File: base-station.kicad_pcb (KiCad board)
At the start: 2 copper layers, 85.7 x 87.2 mm, 53 parts, among them IC1 ATMEGA32-A, P1 HC-05, P2 NRF24L01+, P3 SERIAL, P4 LCD1, P5 LCD1, P6 POWER, Q1 BTEN, SW1 RESET, U1 LP5907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

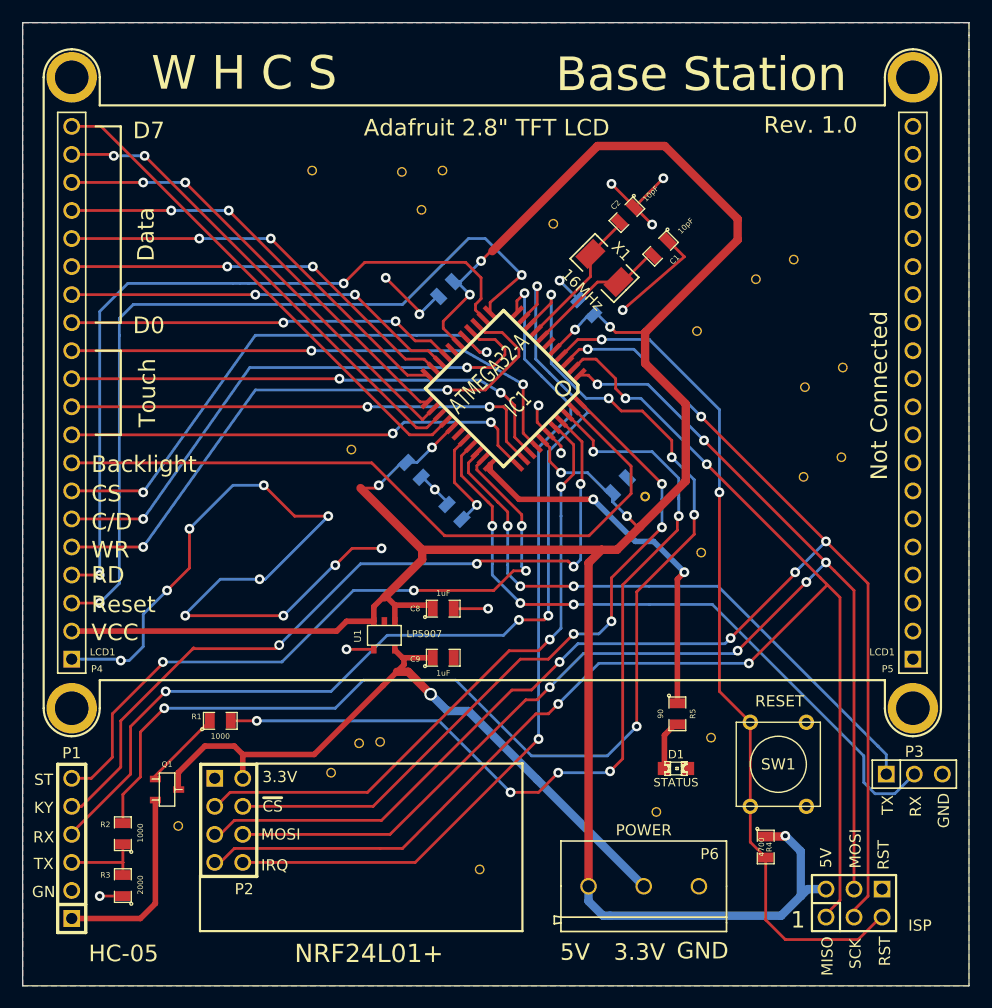
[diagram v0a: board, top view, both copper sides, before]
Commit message: Minor power track edits
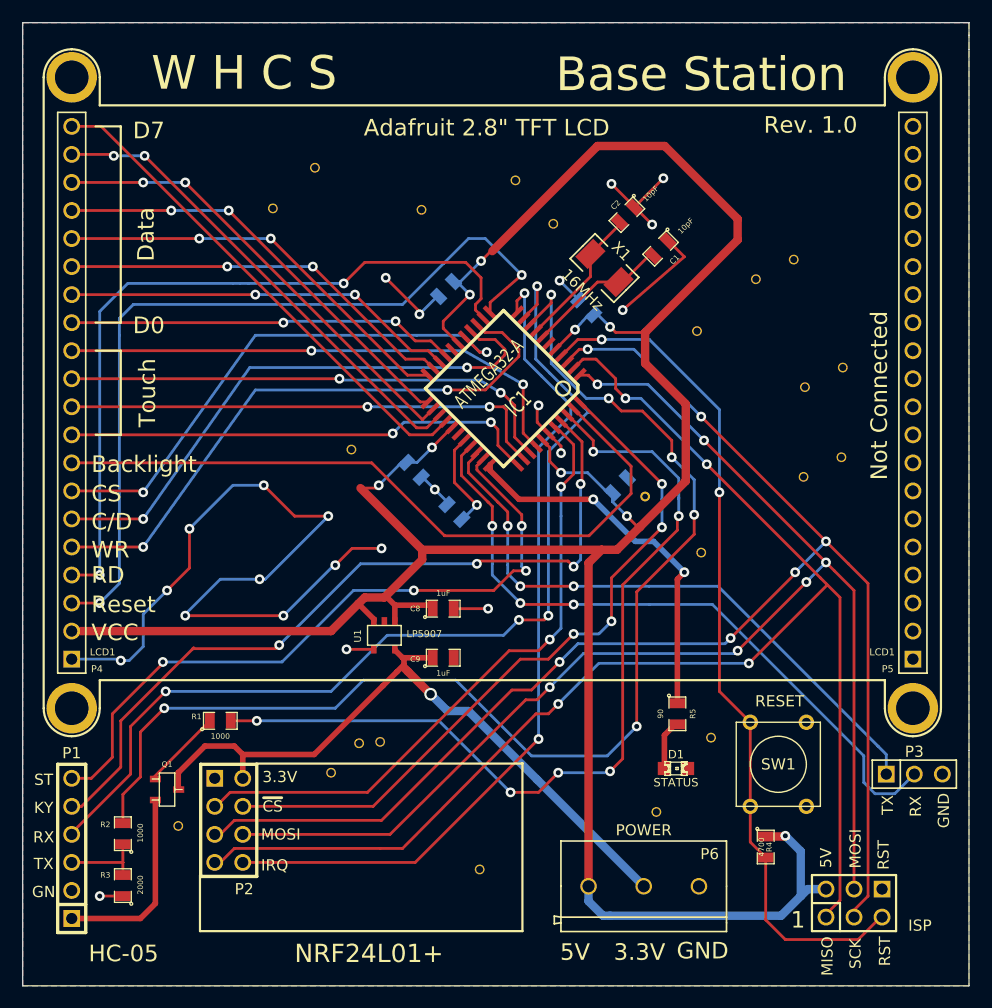
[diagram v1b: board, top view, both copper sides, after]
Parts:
- moved ? 7.88 mm to (116.3, 84.6)
- moved ? 6.66 mm to (134.4, 85.8)
- moved ? 4.94 mm to (112.5, 88.3)
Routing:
- net /VCC: track 245.1 -> 246.6 mm
- net /3V3: track 63.7 -> 63.1 mm
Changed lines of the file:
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@@
     (thickness 1.6)
     (drawings 84)
-    (tracks 696)
+    (tracks 697)
     (zones 0)
     (modules 53)
@@
     (23 F.Mask user)
     (24 Dwgs.User user)
-    (25 Cmts.User user)
+    (25 Cmts.User user hide)
     (26 Eco1.User user)
     (27 Eco2.User user)
@@
   )
   (setup
-    (last_trace_width 0.508)
+    (last_trace_width 0.762)
     (user_trace_width 0.508)
     (user_trace_width 0.762)
@@
   )
   (module gnd-via (layer F.Cu)
-    (at 127.8255 84.8995 90)
+    (at 134.4295 85.7885 90)
     (fp_text reference "" (at 0 0 90) (layer F.SilkS)
       (effects (font (size 1 1) (thickness 0.15)))
@@
   )
   (module gnd-via (layer F.Cu)
-    (at 124.1425 85.0265 90)
+    (at 116.2685 84.6455 90)
     (fp_text reference "" (at 0 0 90) (layer F.SilkS)
       (effects (font (size 1 1) (thickness 0.15)))
@@
   )
   (module gnd-via (layer F.Cu)
-    (at 116.0145 84.8995 90)
+    (at 112.4585 88.3285 90)
     (fp_text reference "" (at 0 0 90) (layer F.SilkS)
       (effects (font (size 1 1) (thickness 0.15)))
@@
     )
     (fp_text value ATMEGA32-A (at 0 1.905 225) (layer F.SilkS)
-      (effects (font (size 1.524 1.016) (thickness 0.2032)))
+      (effects (font (size 1.27 0.889) (thickness 0.2032)))
     )
     (fp_line (start 5.0038 -5.0038) (end 5.0038 5.0038) (layer F.SilkS) (width 0.3048))
@@
   )
   (gr_line (start 175.514 73.914) (end 175.514 137.414) (angle 90) (layer Edge.Cuts) (width 0.1))
+  (segment (start 124.3965 129.9845) (end 124.714 130.302) (width 0.762) (layer F.Cu) (net 1))
+  (segment (start 128.27 133.858) (end 126.746 132.334) (width 0.762) (layer B.Cu) (net 1))
+  (via (at 126.746 132.334) (size 1.143) (drill 0.762) (layers F.Cu B.Cu) (net 1))
+  (segment (start 126.746 132.334) (end 126.6825 132.2705) (width 0.762) (layer F.Cu) (net 1))
+  (segment (start 126.6825 132.2705) (end 124.714 130.302) (width 0.762) (layer F.Cu) (net 1))
+  (segment (start 130.175 133.858) (end 136.398 140.081) (width 0.762) (layer B.Cu) (net 1))
   (segment (start 130.175 133.858) (end 128.27 133.858) (width 0.762) (layer B.Cu) (net 1))
-  (segment (start 136.398 140.081) (end 130.175 133.858) (width 0.762) (layer B.Cu) (net 1))
-  (segment (start 126.6825 132.2705) (end 124.714 130.302) (width 0.762) (layer F.Cu) (net 1))
-  (segment (start 124.714 130.302) (end 123.698 130.302) (width 0.762) (layer F.Cu) (net 1))
-  (segment (start 126.746 132.334) (end 126.6825 132.2705) (width 0.762) (layer F.Cu) (net 1))
-  (via (at 126.746 132.334) (size 1.143) (drill 0.762) (layers F.Cu B.Cu) (net 1))
-  (segment (start 128.27 133.858) (end 126.746 132.334) (width 0.762) (layer B.Cu) (net 1))
   (segment (start 146.05 149.733) (end 136.398 140.081) (width 0.762) (layer B.Cu) (net 1))
   (segment (start 136.398 140.081) (end 136.398 140.081) (width 0.762) (layer B.Cu) (net 1))
@@
   (segment (start 120.396 120.523) (end 130.937 120.523) (width 0.254) (layer B.Cu) (net 15))
   (segment (start 113.03 127.889) (end 120.396 120.523) (width 0.254) (layer B.Cu) (net 15))
-  (via (at 113.03 127.889) (size 0.889) (drill 0.508) (layers F.Cu B.Cu) (net 15))
+  (via (at 113.03 127.889) (size 0.889) (layers F.Cu B.Cu) (net 15))
   (segment (start 112.7125 128.2065) (end 113.03 127.889) (width 0.254) (layer F.Cu) (net 15))
   (segment (start 94.234 142.494) (end 95.123 142.494) (width 0.254) (layer F.Cu) (net 15))
@@
   (segment (start 133.731 117.094) (end 133.731 120.65) (width 0.254) (layer B.Cu) (net 29))
   (segment (start 133.731 120.65) (end 133.731 121.412) (width 0.254) (layer B.Cu) (net 29))
+  (segment (start 121.6025 125.73) (end 121.6025 125.5395) (width 0.508) (layer F.Cu) (net 30))
+  (segment (start 121.6025 125.5395) (end 120.2055 124.1425) (width 0.508) (layer F.Cu) (net 30))
+  (segment (start 122.555 123.571) (end 120.777 123.571) (width 0.762) (layer F.Cu) (net 30))
+  (segment (start 117.729 126.619) (end 94.234 126.619) (width 0.762) (layer F.Cu) (net 30))
+  (segment (start 120.777 123.571) (end 120.2055 124.1425) (width 0.762) (layer F.Cu) (net 30))
+  (segment (start 120.2055 124.1425) (end 117.729 126.619) (width 0.762) (layer F.Cu) (net 30))
   (segment (start 141.05 149.733) (end 141.05 120.443) (width 0.762) (layer F.Cu) (net 30))
   (segment (start 141.05 120.443) (end 142.24 119.253) (width 0.762) (layer F.Cu) (net 30))
@@
   (segment (start 137.541 111.252) (end 138.557 112.268) (width 0.254) (layer F.Cu) (net 30))
   (segment (start 137.541 109.982) (end 137.541 111.252) (width 0.254) (layer F.Cu) (net 30))
-  (segment (start 94.234 126.619) (end 118.237 126.619) (width 0.508) (layer F.Cu) (net 30))
-  (segment (start 119.126 125.73) (end 121.6025 125.73) (width 0.508) (layer F.Cu) (net 30))
-  (segment (start 118.237 126.619) (end 119.126 125.73) (width 0.508) (layer F.Cu) (net 30))
   (segment (start 123.5075 124.2695) (end 126.619 124.2695) (width 0.508) (layer F.Cu) (net 30))
   (segment (start 126.619 124.2695) (end 126.9365 124.587) (width 0.508) (layer F.Cu) (net 30))
@@
   (segment (start 125.984 120.142) (end 122.555 123.571) (width 0.762) (layer F.Cu) (net 30))
   (segment (start 125.984 119.253) (end 125.984 120.142) (width 0.762) (layer F.Cu) (net 30))
-  (segment (start 121.6025 124.3965) (end 121.6025 125.73) (width 0.508) (layer F.Cu) (net 30))
-  (segment (start 122.428 123.571) (end 121.6025 124.3965) (width 0.508) (layer F.Cu) (net 30))
   (segment (start 120.396 113.665) (end 121.793 113.665) (width 0.254) (layer F.Cu) (net 30))
   (segment (start 125.984 119.253) (end 120.396 113.665) (width 0.762) (layer F.Cu) (net 30))

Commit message: Fix LCD and HC-05 wiring mixups. Improved pours
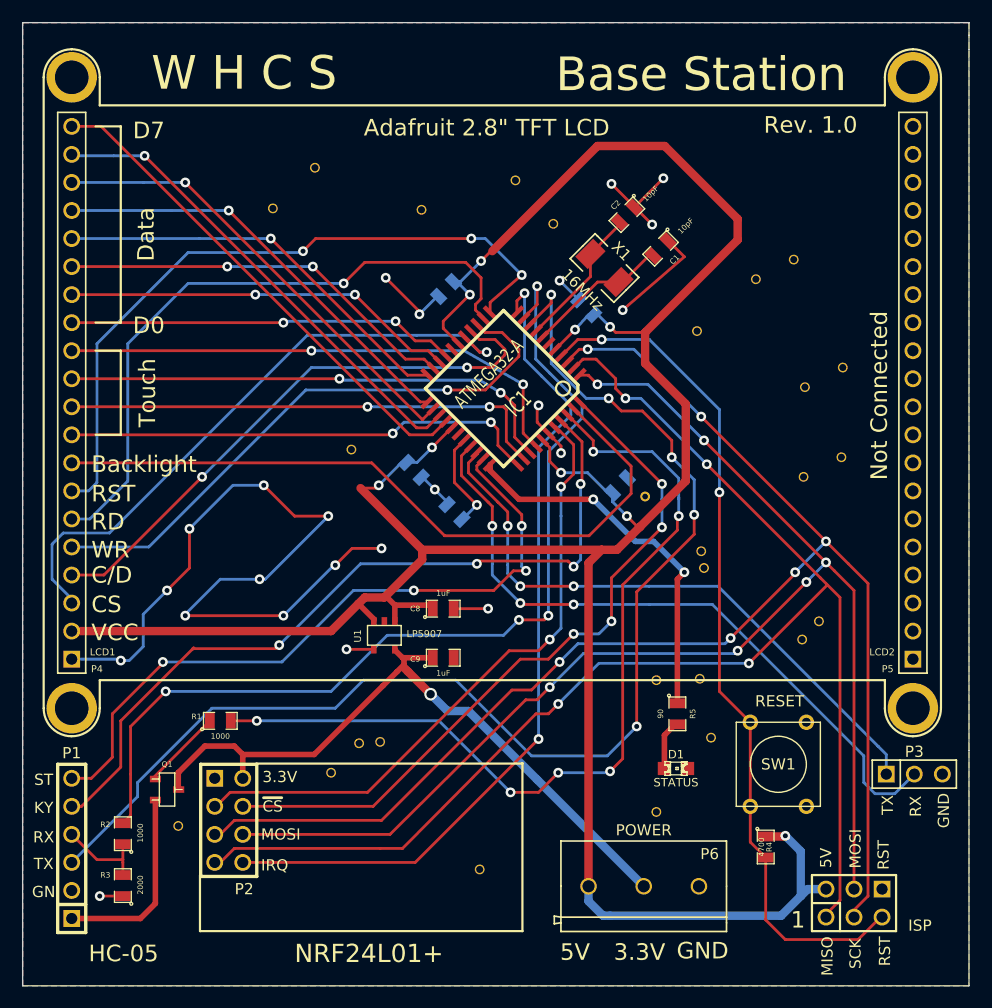
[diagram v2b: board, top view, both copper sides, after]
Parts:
- added ?: , gnd-via, F.Cu at (147.2, 131.1)
- added ?: , gnd-via, F.Cu at (151.1, 130.9)
- added ?: , gnd-via, F.Cu at (151.3, 119.4)
- added ?: , gnd-via, F.Cu at (161.9, 125.7)
- added ?: , gnd-via, F.Cu at (160.4, 127.4)
- P5: value LCD1 -> LCD2
- moved ? 1.42 mm to (151.5, 120.9)
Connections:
- IC1 pad 15: /C/D -> /CD
- P1 pad 3: N-0000015 -> /RX
- P1 pad 4: /TX -> N-0000015
- P4 pad 3: /LRST -> /LCS
- P4 pad 4: /RD -> /CD
- P4 pad 6: /C/D -> /RD
- P4 pad 7: /LCS -> /LRST
- R2 pad 2: /RX -> /TX
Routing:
- net /CD: track 0.00 -> 51.7 mm, vias 0 -> 2
- net /C/D: track 51.1 -> 0.00 mm, vias 2 -> 0
- net /LRST: track 74.7 -> 63.7 mm, vias 2 -> 3
- net /RD: track 67.8 -> 58.8 mm, vias 2 -> 1
- net /LCS: track 48.1 -> 56.4 mm, vias 2 -> 1
- net /TX: track 91.0 -> 87.4 mm
- net /RX: track 112.3 -> 115.2 mm, vias 6 -> 5
- net /WR: track 54.4 -> 52.9 mm, vias 2 -> 1
- net N-0000015: track 7.56 -> 8.38 mm
- net /D6: vias 2 -> 1
- net /D5: vias 2 -> 1
- net /D4: vias 2 -> 1
- net /D3: vias 2 -> 1
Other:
- board text removed: "Reset"

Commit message: More ground pour vias. Silk screen adjustments
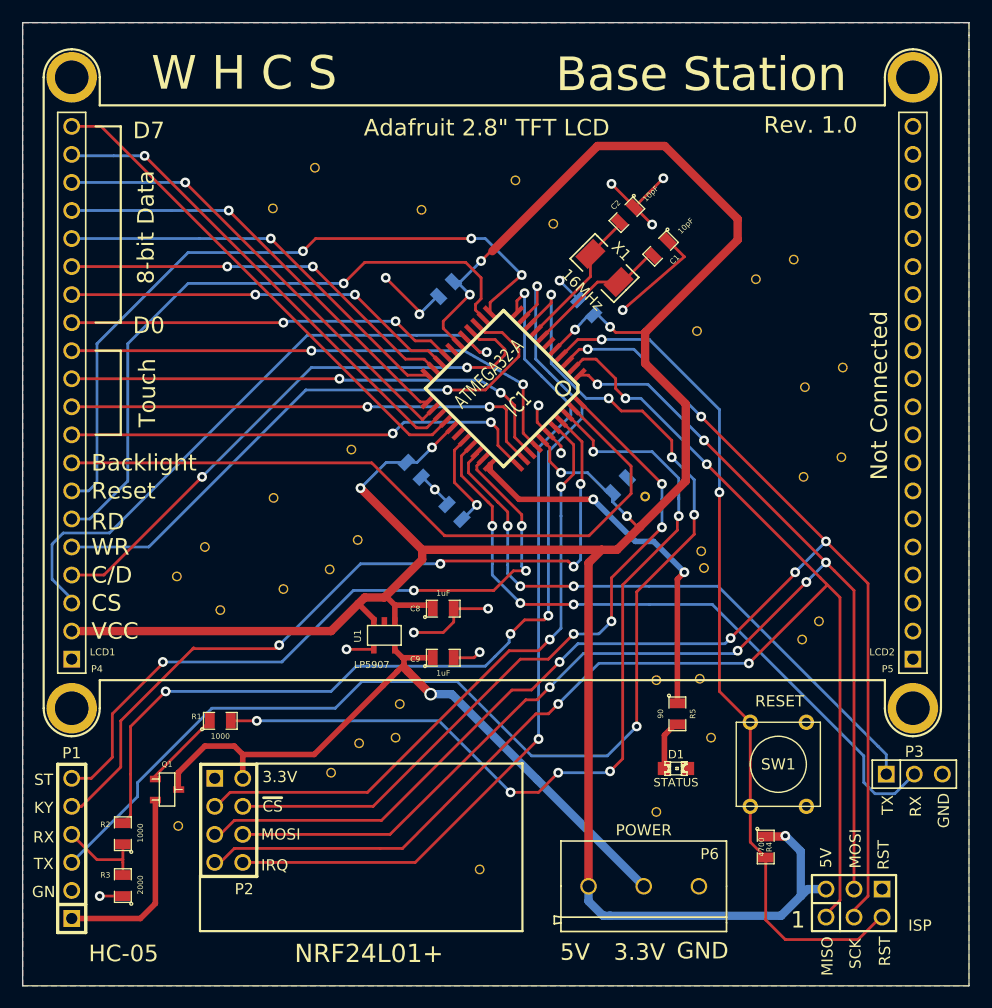
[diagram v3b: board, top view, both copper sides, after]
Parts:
- added ?: , gnd-via, F.Cu at (107.7, 124.7)
- added ?: , gnd-via, F.Cu at (120.1, 118.4)
- added ?: , gnd-via, F.Cu at (117.6, 121.0)
- added ?: , gnd-via, F.Cu at (113.4, 122.8)
- added ?: , gnd-via, F.Cu at (112.5, 114.6)
- added ?: , gnd-via, F.Cu at (103.8, 121.7)
- added ?: , gnd-via, F.Cu at (106.3, 119.0)
- added ?: , gnd-via, F.Cu at (123.6, 136.3)
- moved ? 3.86 mm to (124.0, 133.2)
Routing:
- net GND: track 116.2 -> 52.1 mm, vias 23 -> 15
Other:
- board text added: "8-bit Data"
- board text added: "Reset"
- board text removed: "Data"

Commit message: Moved HC-05 NMOS to low-side
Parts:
- added ?: , gnd-via, F.Cu at (101.9, 135.9)
- added ?: , gnd-via, F.Cu at (102.2, 140.3)
- moved Q1 9.29 mm to (99.4, 149.6), turned to 90 degrees
- moved ? 8.02 mm to (96.9, 148.2)
- moved R3 5.38 mm to (101.6, 145.0), turned to 270 degrees
- moved ? 5.00 mm to (113.7, 136.5)
- renumbered ISP to ISP1
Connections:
- P1 pad 1: N-0000017 (its old number) -> /3V3
- P1 pad 2: GND -> /HC_GND
- Q1 pad 2: /3V3 -> /HC_GND
- Q1 pad 3: N-0000017 (its old number) -> GND
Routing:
- net /3V3: track 63.1 -> 83.1 mm
- net N-0000017 (its old number): track 17.5 -> 0.00 mm
- net N-0000014: track 7.42 -> 19.1 mm
- net /HC_GND: track 0.00 -> 4.36 mm
- net GND: track 52.1 -> 50.0 mm, vias 15 -> 14
- net N-0000017: track 8.38 -> 10.3 mm
